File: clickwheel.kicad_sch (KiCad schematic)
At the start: 4 parts

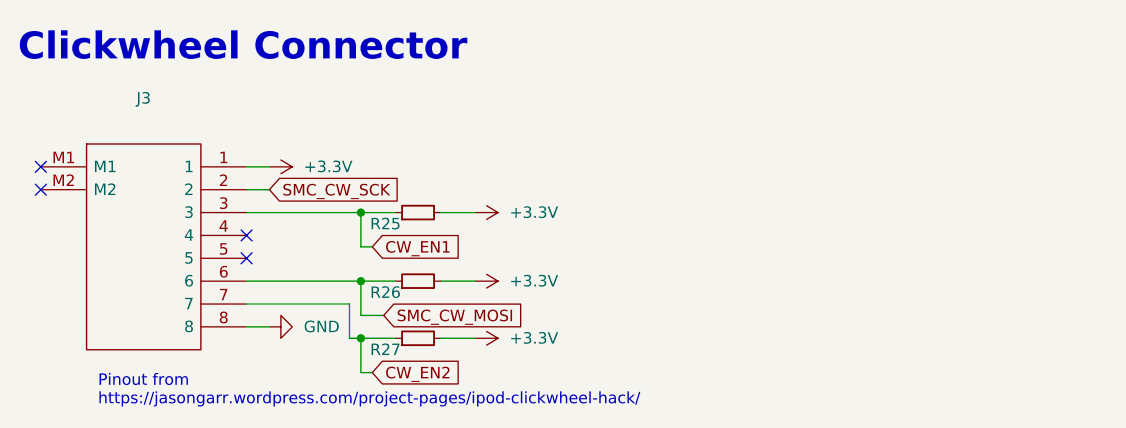
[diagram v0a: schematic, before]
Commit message: layout: add testpoints, extra mounting hole, grounding clips
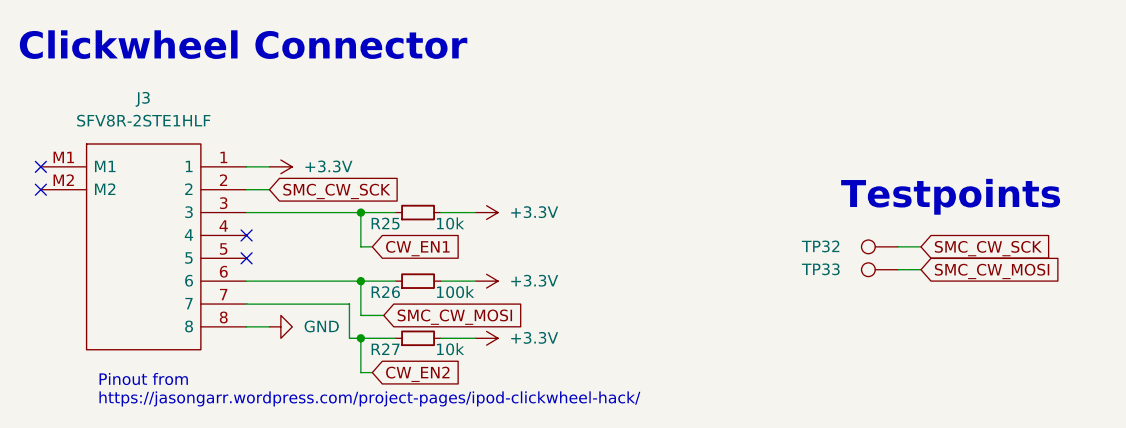
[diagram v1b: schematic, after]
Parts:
- added TP32, TP33: TestPoint, TestPoint:TestPoint_Pad_D1.5mm, symbol Connector:TestPoint
- J3: value (none) -> SFV8R-2STE1HLF; footprint (none) -> Gigahawk:SFV8R2STE1HLF
- R25, R27: value (none) -> 10k; footprint (none) -> Resistor_SMD:R_0402_1005Metric
- R26: value (none) -> 100k; footprint (none) -> Resistor_SMD:R_0402_1005Metric
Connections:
- net SMC_CW_MOSI: now also TP33.1
- net SMC_CW_SCK: now also TP32.1
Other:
- note added: "Testpoints"
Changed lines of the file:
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@@
+    (stroke (width 0) (type default) (color 0 0 0 0))
+  )
+  (wire (pts (xy 190.5 97.79) (xy 193.04 97.79))
     (stroke (width 0) (type default) (color 0 0 0 0))
   )
@@
     (stroke (width 0) (type default) (color 0 0 0 0))
   )
+  (wire (pts (xy 190.5 100.33) (xy 193.04 100.33))
+    (stroke (width 0) (type default) (color 0 0 0 0))
+  )
   (wire (pts (xy 130.81 93.98) (xy 134.62 93.98))
     (stroke (width 0) (type default) (color 0 0 0 0))
@@
   )
   (text "Clickwheel Connector" (at 92.71 77.47 0)
+    (effects (font (size 3 3) (thickness 0.6) bold) (justify left bottom))
+  )
+  (text "Testpoints" (at 184.15 93.98 0)
     (effects (font (size 3 3) (thickness 0.6) bold) (justify left bottom))
   )
@@
     )
   )
+  (global_label "SMC_CW_MOSI" (shape input) (at 193.04 100.33 0) (fields_autoplaced)
+    (effects (font (size 1.27 1.27)) (justify left))
+    (property "Intersheet References" "${INTERSHEET_REFS}" (id 0) (at 208.6369 100.2506 0)
+      (effects (font (size 1.27 1.27)) (justify left) hide)
+    )
+  )
   (global_label "SMC_CW_SCK" (shape input) (at 120.65 91.44 0) (fields_autoplaced)
     (effects (font (size 1.27 1.27)) (justify left))
@@
     )
   )
+  (global_label "SMC_CW_SCK" (shape input) (at 193.04 97.79 0) (fields_autoplaced)
+    (effects (font (size 1.27 1.27)) (justify left))
+    (property "Intersheet References" "${INTERSHEET_REFS}" (id 0) (at 207.7902 97.7106 0)
+      (effects (font (size 1.27 1.27)) (justify left) hide)
+    )
+  )
   (global_label "SMC_CW_MOSI" (shape input) (at 133.35 105.41 0) (fields_autoplaced)
     (effects (font (size 1.27 1.27)) (justify left))
@@
     )
   )
+  (symbol (lib_id "Connector:TestPoint") (at 190.5 97.79 90) (unit 1)
+    (in_bom yes) (on_board yes)
+    (property "Reference" "TP32" (id 0) (at 184.15 97.79 90)
+      (effects (font (size 1.27 1.27)) (justify left))
+    )
+    (property "Value" "TestPoint" (id 1) (at 188.4679 95.25 0)
+      (effects (font (size 1.27 1.27)) (justify left) hide)
+    )
+    (property "Footprint" "TestPoint:TestPoint_Pad_D1.5mm" (id 2) (at 190.5 92.71 0)
+      (effects (font (size 1.27 1.27)) hide)
+    )
+    (property "Datasheet" "~" (id 3) (at 190.5 92.71 0)
+      (effects (font (size 1.27 1.27)) hide)
+    )
+    (pin "1")
+  )
   (symbol (lib_id "power:+3.3V") (at 143.51 93.98 270) (unit 1)
     (in_bom yes) (on_board yes) (fields_autoplaced)
@@
     (in_bom yes) (on_board yes) (fields_autoplaced)
     (property "Reference" "J3" (id 0) (at 106.68 81.28 0))
-    (property "Value" "" (id 1) (at 106.68 83.82 0))
-    (property "Footprint" "" (id 2) (at 114.3 86.36 0)
+    (property "Value" "SFV8R-2STE1HLF" (id 1) (at 106.68 83.82 0))
+    (property "Footprint" "Gigahawk:SFV8R2STE1HLF" (id 2) (at 114.3 86.36 0)
       (effects (font (size 1.27 1.27)) (justify left) hide)
     )
@@
       (effects (font (size 1.27 1.27)) (justify left))
     )
-    (property "Value" "" (id 1) (at 139.065 95.25 90)
-      (effects (font (size 1.27 1.27)) (justify right))
-    )
-    (property "Footprint" "" (id 2) (at 137.16 93.98 0)
+    (property "Value" "10k" (id 1) (at 139.065 95.25 90)
+      (effects (font (size 1.27 1.27)) (justify right))
+    )
+    (property "Footprint" "Resistor_SMD:R_0402_1005Metric" (id 2) (at 137.16 93.98 0)
       (effects (font (size 1.27 1.27)) hide)
     )
@@
     (pin "2")
   )
+  (symbol (lib_id "Connector:TestPoint") (at 190.5 100.33 90) (unit 1)
+    (in_bom yes) (on_board yes)
+    (property "Reference" "TP33" (id 0) (at 184.15 100.33 90)
+      (effects (font (size 1.27 1.27)) (justify left))
+    )
+    (property "Value" "TestPoint" (id 1) (at 188.4679 97.79 0)
+      (effects (font (size 1.27 1.27)) (justify left) hide)
+    )
+    (property "Footprint" "TestPoint:TestPoint_Pad_D1.5mm" (id 2) (at 190.5 95.25 0)
+      (effects (font (size 1.27 1.27)) hide)
+    )
+    (property "Datasheet" "~" (id 3) (at 190.5 95.25 0)
+      (effects (font (size 1.27 1.27)) hide)
+    )
+    (pin "1")
+  )
   (symbol (lib_id "Device:R_Small") (at 137.16 107.95 90) (unit 1)
     (in_bom yes) (on_board yes)
@@
       (effects (font (size 1.27 1.27)) (justify left))
     )
-    (property "Value" "" (id 1) (at 139.065 109.22 90)
-      (effects (font (size 1.27 1.27)) (justify right))
-    )
-    (property "Footprint" "" (id 2) (at 137.16 107.95 0)
+    (property "Value" "10k" (id 1) (at 139.065 109.22 90)
+      (effects (font (size 1.27 1.27)) (justify right))
+    )
+    (property "Footprint" "Resistor_SMD:R_0402_1005Metric" (id 2) (at 137.16 107.95 0)
       (effects (font (size 1.27 1.27)) hide)
     )
@@
       (effects (font (size 1.27 1.27)) (justify left))
     )
-    (property "Value" "" (id 1) (at 139.065 102.87 90)
-      (effects (font (size 1.27 1.27)) (justify right))
-    )
-    (property "Footprint" "" (id 2) (at 137.16 101.6 0)
-      (effects (font (size 1.27 1.27)) hide)
-    )
+    (property "Value" "100k" (id 1) (at 139.065 102.87 90)
+      (effects (font (size 1.27 1.27)) (justify right))
+    )
+    (property "Footprint" "Resistor_SMD:R_0402_1005Metric" (id 2) (at 137.16 101.6 0)
+      (effects (font (size 1.27 1.27)) hide)
+    )

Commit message: ci: prepare files for CI
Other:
- title: (none) -> piPod IO/SMC Board
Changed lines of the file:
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@@
 (kicad_sch (version 20211123) (generator eeschema)
   (paper "A4")
+  (title_block
+    (title "piPod IO/SMC Board")
+    (date "${DATE}")
+    (rev "%{TAG} (${REVISION})")
+  )
   (junction (at 130.81 107.95) (diameter 0) (color 0 0 0 0)
   )

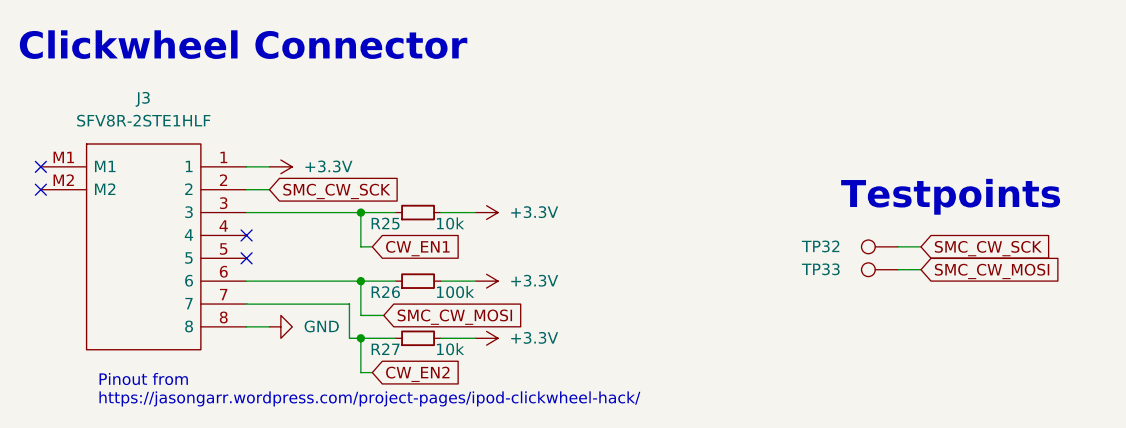
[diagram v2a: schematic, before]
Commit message: ci: test marking parts in sch for bom
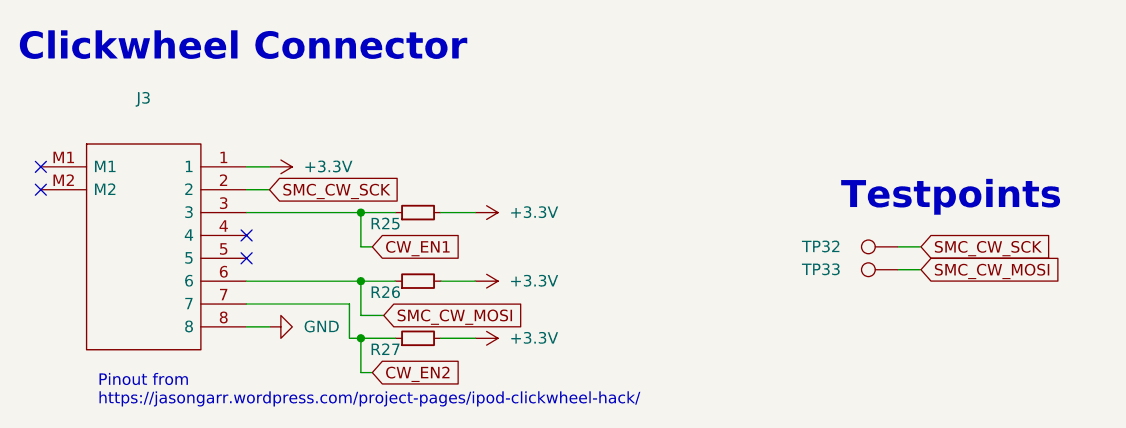
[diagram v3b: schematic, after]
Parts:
- J3: value SFV8R-2STE1HLF -> (none); footprint Gigahawk:SFV8R2STE1HLF -> (none)
- R25, R27: value 10k -> (none); footprint Resistor_SMD:R_0402_1005Metric -> (none)
- R26: value 100k -> (none); footprint Resistor_SMD:R_0402_1005Metric -> (none)
- TP32, TP33: value TestPoint -> (none); footprint TestPoint:TestPoint_Pad_D1.5mm -> (none)
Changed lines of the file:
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@@
       (effects (font (size 1.27 1.27)) (justify left))
     )
-    (property "Value" "TestPoint" (id 1) (at 188.4679 95.25 0)
+    (property "Value" "" (id 1) (at 188.4679 95.25 0)
       (effects (font (size 1.27 1.27)) (justify left) hide)
     )
-    (property "Footprint" "TestPoint:TestPoint_Pad_D1.5mm" (id 2) (at 190.5 92.71 0)
+    (property "Footprint" "" (id 2) (at 190.5 92.71 0)
       (effects (font (size 1.27 1.27)) hide)
     )
@@
     (in_bom yes) (on_board yes) (fields_autoplaced)
     (property "Reference" "J3" (id 0) (at 106.68 81.28 0))
-    (property "Value" "SFV8R-2STE1HLF" (id 1) (at 106.68 83.82 0))
-    (property "Footprint" "Gigahawk:SFV8R2STE1HLF" (id 2) (at 114.3 86.36 0)
+    (property "Value" "" (id 1) (at 106.68 83.82 0))
+    (property "Footprint" "" (id 2) (at 114.3 86.36 0)
       (effects (font (size 1.27 1.27)) (justify left) hide)
     )
@@
       (effects (font (size 1.27 1.27)) (justify left))
     )
-    (property "Value" "10k" (id 1) (at 139.065 95.25 90)
+    (property "Value" "" (id 1) (at 139.065 95.25 90)
       (effects (font (size 1.27 1.27)) (justify right))
     )
-    (property "Footprint" "Resistor_SMD:R_0402_1005Metric" (id 2) (at 137.16 93.98 0)
+    (property "Footprint" "" (id 2) (at 137.16 93.98 0)
       (effects (font (size 1.27 1.27)) hide)
     )
@@
       (effects (font (size 1.27 1.27)) (justify left))
     )
-    (property "Value" "TestPoint" (id 1) (at 188.4679 97.79 0)
+    (property "Value" "" (id 1) (at 188.4679 97.79 0)
       (effects (font (size 1.27 1.27)) (justify left) hide)
     )
-    (property "Footprint" "TestPoint:TestPoint_Pad_D1.5mm" (id 2) (at 190.5 95.25 0)
+    (property "Footprint" "" (id 2) (at 190.5 95.25 0)
       (effects (font (size 1.27 1.27)) hide)
     )
@@
       (effects (font (size 1.27 1.27)) (justify left))
     )
-    (property "Value" "10k" (id 1) (at 139.065 109.22 90)
+    (property "Value" "" (id 1) (at 139.065 109.22 90)
       (effects (font (size 1.27 1.27)) (justify right))
     )
-    (property "Footprint" "Resistor_SMD:R_0402_1005Metric" (id 2) (at 137.16 107.95 0)
+    (property "Footprint" "" (id 2) (at 137.16 107.95 0)
       (effects (font (size 1.27 1.27)) hide)
     )
@@
       (effects (font (size 1.27 1.27)) (justify left))
     )
-    (property "Value" "100k" (id 1) (at 139.065 102.87 90)
+    (property "Value" "" (id 1) (at 139.065 102.87 90)
       (effects (font (size 1.27 1.27)) (justify right))
     )
-    (property "Footprint" "Resistor_SMD:R_0402_1005Metric" (id 2) (at 137.16 101.6 0)
+    (property "Footprint" "" (id 2) (at 137.16 101.6 0)
       (effects (font (size 1.27 1.27)) hide)
     )
